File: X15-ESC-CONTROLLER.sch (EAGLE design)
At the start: 27 parts, among them IC1 OP-AMP, J1 3V3 -SWCLK-GND-SWDIO- NRST, Y1 ECS-80-S-4X

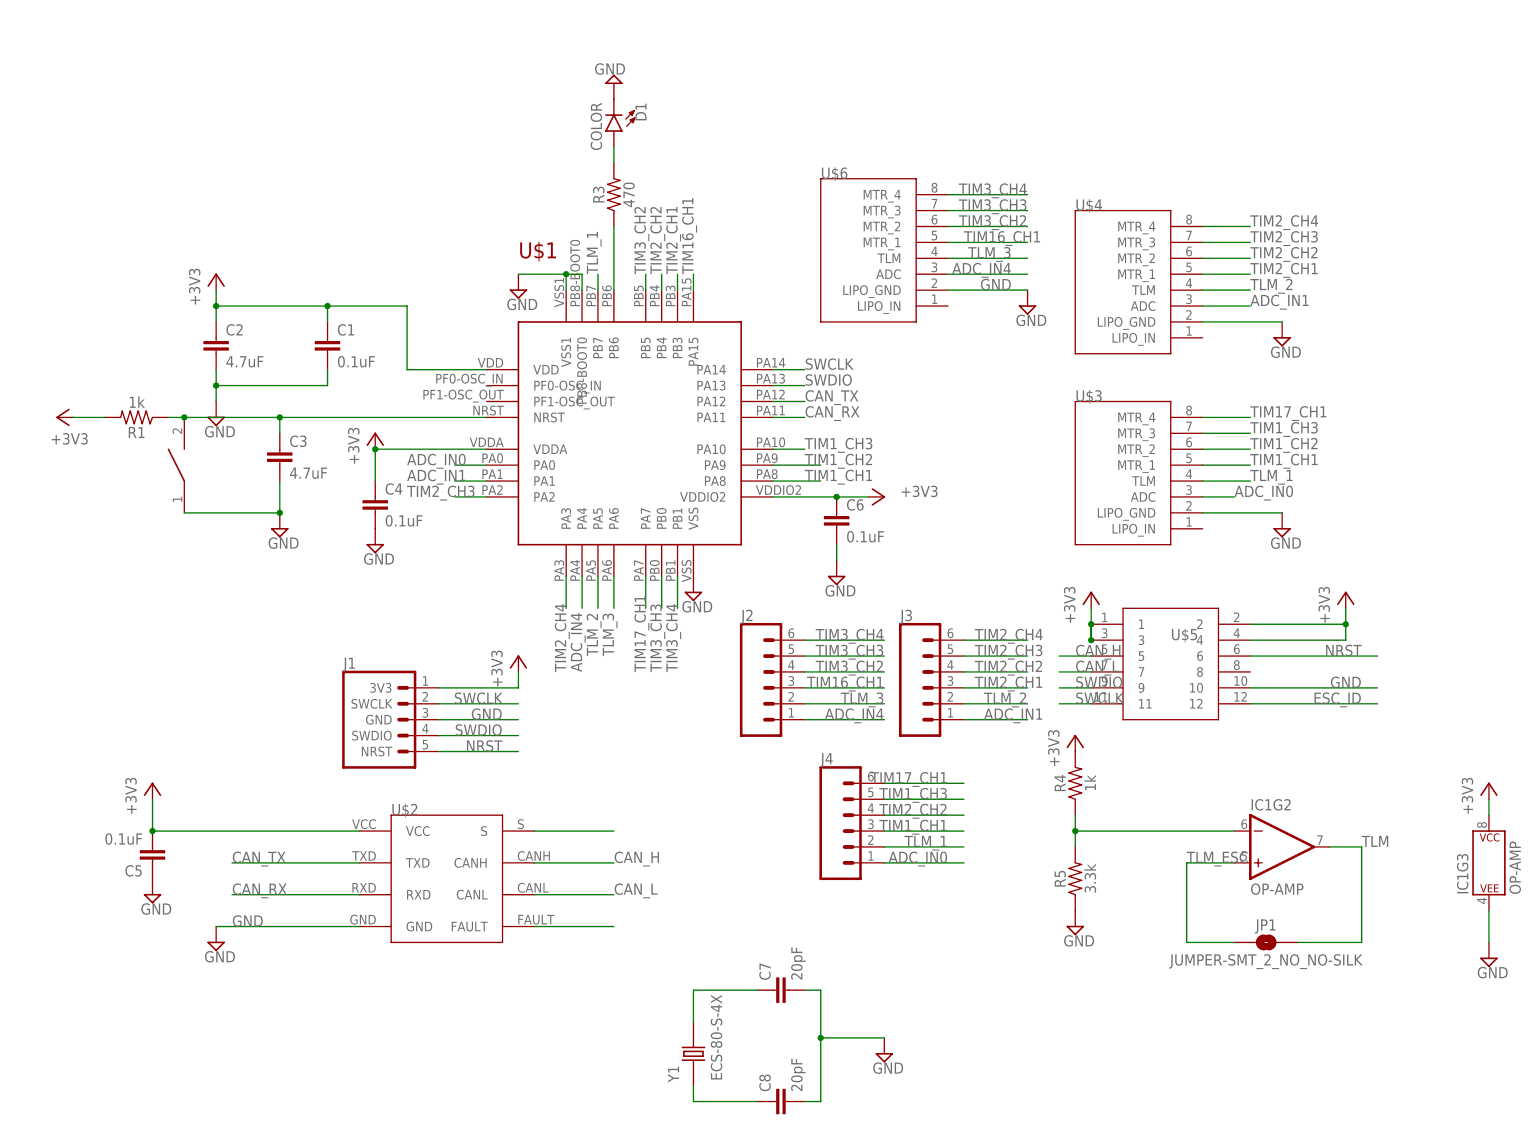
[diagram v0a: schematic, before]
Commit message: Fix some traces with polygons
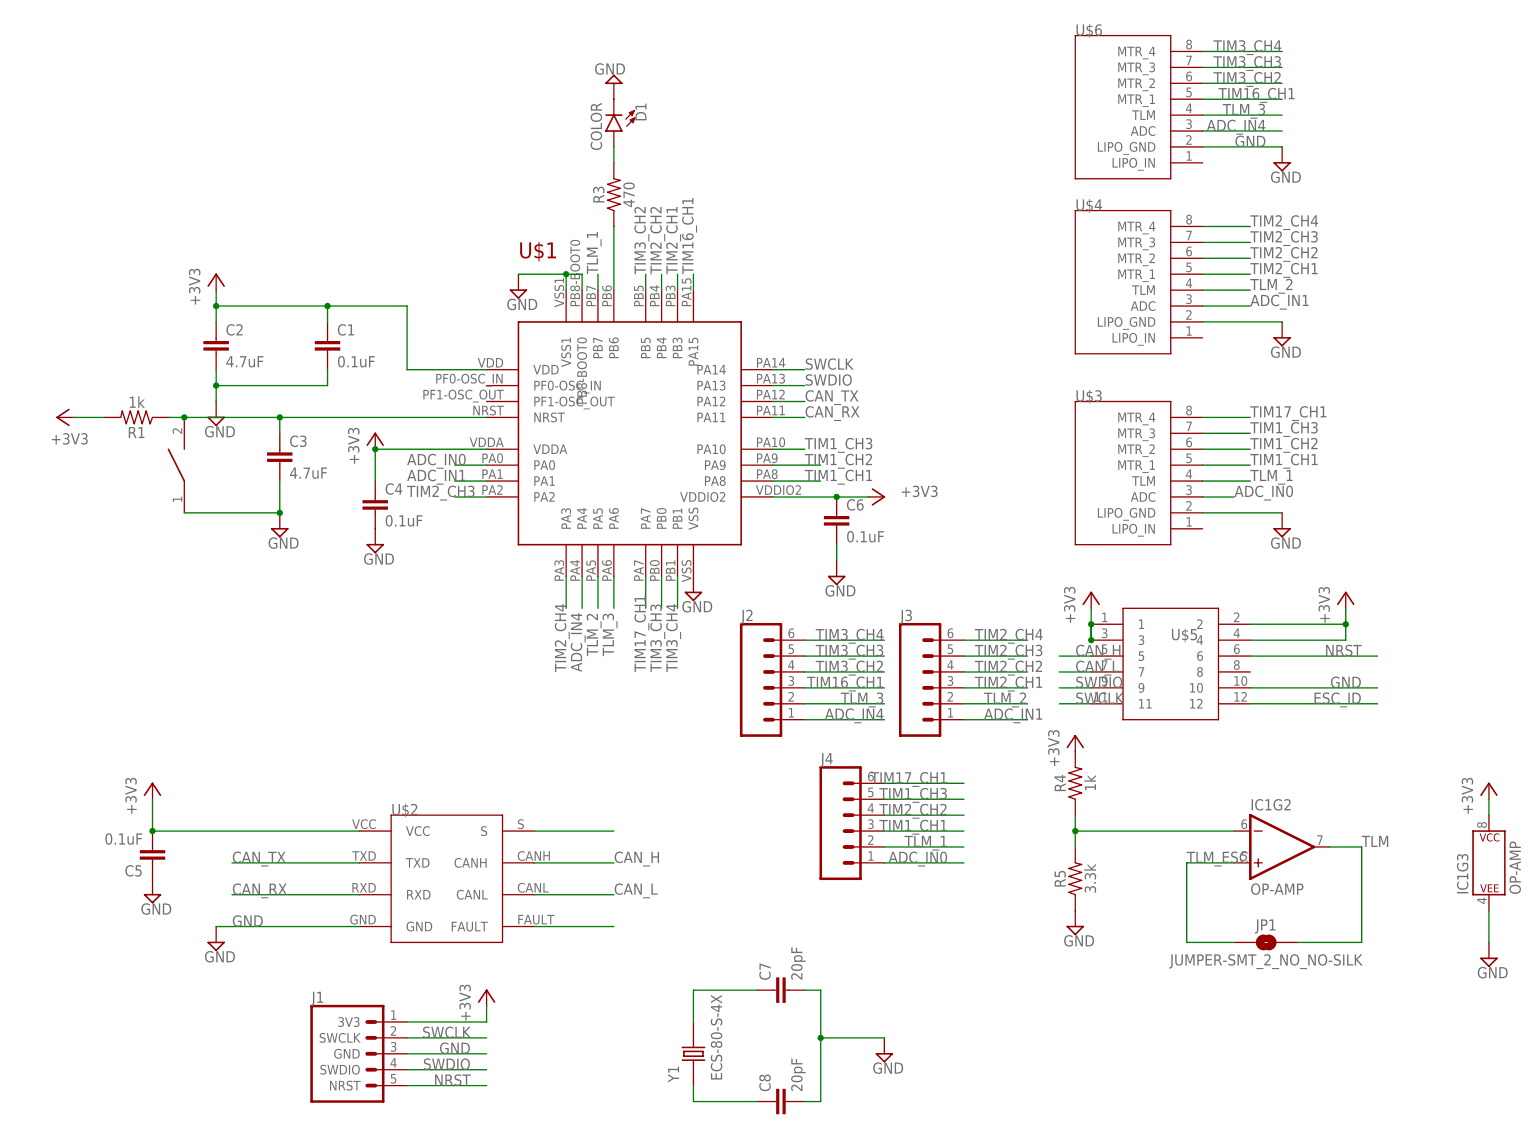
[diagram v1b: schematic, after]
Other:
- moved on the sheet: J1, U$6
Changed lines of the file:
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@@
 <attribute name="VALUE" x="-60.325" y="1.905" size="1.778" layer="96"/>
 </instance>
-<instance part="J1" gate="G$1" x="-20.32" y="33.02" smashed="yes">
-<attribute name="NAME" x="-27.94" y="41.148" size="1.778" layer="95" font="vector"/>
+<instance part="J1" gate="G$1" x="-25.4" y="-20.32" smashed="yes">
+<attribute name="NAME" x="-33.02" y="-12.192" size="1.778" layer="95" font="vector"/>
 </instance>
 <instance part="+3V5" gate="G$1" x="58.42" y="68.58" smashed="yes" rot="R270">
@@
 <attribute name="VALUE" x="153.035" y="-8.255" size="1.778" layer="96"/>
 </instance>
-<instance part="+3V11" gate="G$1" x="0" y="43.18" smashed="yes">
-<attribute name="VALUE" x="-2.54" y="38.1" size="1.778" layer="96" rot="R90"/>
-</instance>
-<instance part="U$6" gate="G$1" x="55.88" y="106.68" smashed="yes">
-<attribute name="NAME" x="48.26" y="119.38" size="1.778" layer="95"/>
-</instance>
-<instance part="SUPPLY15" gate="GND" x="81.28" y="99.06" smashed="yes">
-<attribute name="VALUE" x="79.375" y="95.885" size="1.778" layer="96"/>
+<instance part="+3V11" gate="G$1" x="-5.08" y="-10.16" smashed="yes">
+<attribute name="VALUE" x="-7.62" y="-15.24" size="1.778" layer="96" rot="R90"/>
+</instance>
+<instance part="U$6" gate="G$1" x="96.52" y="129.54" smashed="yes">
+<attribute name="NAME" x="88.9" y="142.24" size="1.778" layer="95"/>
+</instance>
+<instance part="SUPPLY15" gate="GND" x="121.92" y="121.92" smashed="yes">
+<attribute name="VALUE" x="120.015" y="118.745" size="1.778" layer="96"/>
 </instance>
 <instance part="Y1" gate="G$1" x="27.94" y="-20.32" smashed="yes" rot="R90">
@@
 <segment>
 <pinref part="J1" gate="G$1" pin="3V3"/>
-<wire x1="-12.7" y1="38.1" x2="0" y2="38.1" width="0.1524" layer="91"/>
+<wire x1="-17.78" y1="-15.24" x2="-5.08" y2="-15.24" width="0.1524" layer="91"/>
 <pinref part="+3V11" gate="G$1" pin="+3V3"/>
-<wire x1="0" y1="40.64" x2="0" y2="38.1" width="0.1524" layer="91"/>
+<wire x1="-5.08" y1="-12.7" x2="-5.08" y2="-15.24" width="0.1524" layer="91"/>
 </segment>
 <segment>
@@
 <segment>
 <pinref part="J1" gate="G$1" pin="GND"/>
-<wire x1="-12.7" y1="33.02" x2="0" y2="33.02" width="0.1524" layer="91"/>
-<label x="-2.54" y="33.02" size="1.778" layer="95" align="bottom-right"/>
+<wire x1="-17.78" y1="-20.32" x2="-5.08" y2="-20.32" width="0.1524" layer="91"/>
+<label x="-7.62" y="-20.32" size="1.778" layer="95" align="bottom-right"/>
 </segment>
 <segment>
@@
 <segment>
 <pinref part="U$6" gate="G$1" pin="LIPO_GND"/>
-<wire x1="68.58" y1="101.6" x2="81.28" y2="101.6" width="0.1524" layer="91"/>
-<label x="78.74" y="101.6" size="1.778" layer="95" align="bottom-right"/>
+<wire x1="109.22" y1="124.46" x2="121.92" y2="124.46" width="0.1524" layer="91"/>
+<label x="119.38" y="124.46" size="1.778" layer="95" align="bottom-right"/>
 <pinref part="SUPPLY15" gate="GND" pin="GND"/>
 </segment>
@@
 <segment>
 <pinref part="J1" gate="G$1" pin="NRST"/>
-<wire x1="-12.7" y1="27.94" x2="0" y2="27.94" width="0.1524" layer="91"/>
-<label x="-2.54" y="27.94" size="1.778" layer="95" align="bottom-right"/>
+<wire x1="-17.78" y1="-25.4" x2="-5.08" y2="-25.4" width="0.1524" layer="91"/>
+<label x="-7.62" y="-25.4" size="1.778" layer="95" align="bottom-right"/>
 </segment>
 <segment>
@@
 <segment>
 <pinref part="J1" gate="G$1" pin="SWDIO"/>
-<wire x1="-12.7" y1="30.48" x2="0" y2="30.48" width="0.1524" layer="91"/>
-<label x="-2.54" y="30.48" size="1.778" layer="95" align="bottom-right"/>
+<wire x1="-17.78" y1="-22.86" x2="-5.08" y2="-22.86" width="0.1524" layer="91"/>
+<label x="-7.62" y="-22.86" size="1.778" layer="95" align="bottom-right"/>
 </segment>
 <segment>
@@
 <segment>
 <pinref part="J1" gate="G$1" pin="SWCLK"/>
-<wire x1="-12.7" y1="35.56" x2="0" y2="35.56" width="0.1524" layer="91"/>
-<label x="-2.54" y="35.56" size="1.778" layer="95" align="bottom-right"/>
+<wire x1="-17.78" y1="-17.78" x2="-5.08" y2="-17.78" width="0.1524" layer="91"/>
+<label x="-7.62" y="-17.78" size="1.778" layer="95" align="bottom-right"/>
 </segment>
 <segment>
@@
 <segment>
 <pinref part="U$6" gate="G$1" pin="ADC"/>
-<wire x1="68.58" y1="104.14" x2="81.28" y2="104.14" width="0.1524" layer="91"/>
-<label x="78.74" y="104.14" size="1.778" layer="95" align="bottom-right"/>
+<wire x1="109.22" y1="127" x2="121.92" y2="127" width="0.1524" layer="91"/>
+<label x="119.38" y="127" size="1.778" layer="95" align="bottom-right"/>
 </segment>
 <segment>
@@
 <segment>
 <pinref part="U$6" gate="G$1" pin="TLM"/>
-<wire x1="68.58" y1="106.68" x2="81.28" y2="106.68" width="0.1524" layer="91"/>
-<label x="78.74" y="106.68" size="1.778" layer="95" align="bottom-right"/>
+<wire x1="109.22" y1="129.54" x2="121.92" y2="129.54" width="0.1524" layer="91"/>
+<label x="119.38" y="129.54" size="1.778" layer="95" align="bottom-right"/>
 </segment>
 <segment>
@@
 <segment>
 <pinref part="U$6" gate="G$1" pin="MTR_3"/>
-<wire x1="68.58" y1="114.3" x2="81.28" y2="114.3" width="0.1524" layer="91"/>
-<label x="81.28" y="114.3" size="1.778" layer="95" align="bottom-right"/>
+<wire x1="109.22" y1="137.16" x2="121.92" y2="137.16" width="0.1524" layer="91"/>
+<label x="121.92" y="137.16" size="1.778" layer="95" align="bottom-right"/>
 </segment>
 <segment>
@@
 <segment>
 <pinref part="U$6" gate="G$1" pin="MTR_4"/>
-<wire x1="68.58" y1="116.84" x2="81.28" y2="116.84" width="0.1524" layer="91"/>
-<label x="81.28" y="116.84" size="1.778" layer="95" align="bottom-right"/>
+<wire x1="109.22" y1="139.7" x2="121.92" y2="139.7" width="0.1524" layer="91"/>
+<label x="121.92" y="139.7" size="1.778" layer="95" align="bottom-right"/>
 </segment>
 <segment>
@@
 <segment>
 <pinref part="U$6" gate="G$1" pin="MTR_2"/>
-<wire x1="68.58" y1="111.76" x2="81.28" y2="111.76" width="0.1524" layer="91"/>
-<label x="81.28" y="111.76" size="1.778" layer="95" align="bottom-right"/>
+<wire x1="109.22" y1="134.62" x2="121.92" y2="134.62" width="0.1524" layer="91"/>
+<label x="121.92" y="134.62" size="1.778" layer="95" align="bottom-right"/>
 </segment>
 <segment>
@@
 <segment>
 <pinref part="U$6" gate="G$1" pin="MTR_1"/>
-<wire x1="68.58" y1="109.22" x2="81.28" y2="109.22" width="0.1524" layer="91"/>
-<label x="71.12" y="109.22" size="1.778" layer="95"/>
-</segment>
-<segment>
+<wire x1="109.22" y1="132.08" x2="121.92" y2="132.08" width="0.1524" layer="91"/>
+<label x="111.76" y="132.08" size="1.778" layer="95"/>
+</segment>
+<segment>

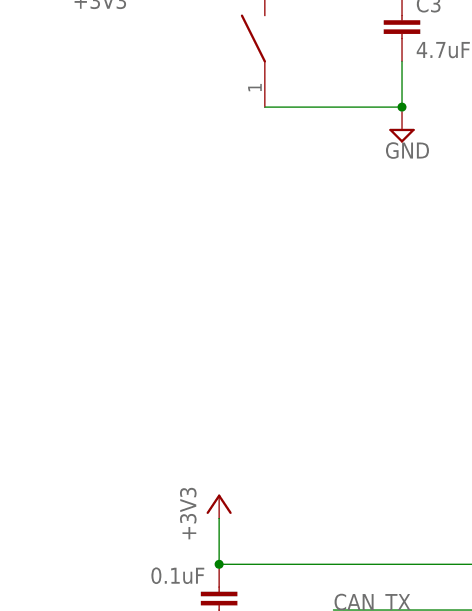
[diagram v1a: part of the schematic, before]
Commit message: Add 3.3V testing LED
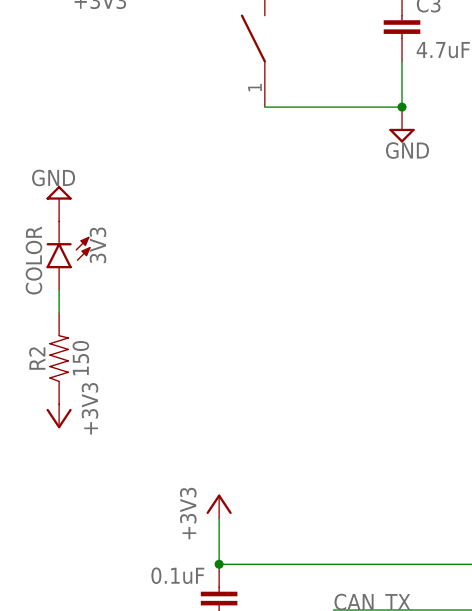
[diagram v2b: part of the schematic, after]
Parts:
- added 3V3: COLOR, X15-ESC-Controller-Parts-Library:LED-0805
- added R2: 150, SparkFun-Resistors:1KOHM-0603-1/10W-1%
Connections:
- new net N$1: 3V3.A, R2.2
- net +3V3: now also R2.1
- net GND: now also 3V3.C
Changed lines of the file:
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@@
 <part name="U$7" library="X15-ESC-Controller-Parts-Library" deviceset="DISCRETECOMPONENTS_SWITCH" device="" package3d_urn="urn:adsk.eagle:package:24384574/2"/>
 <part name="D1" library="X15-ESC-Controller-Parts-Library" deviceset="LED-0805" device="" value="COLOR"/>
+<part name="3V3" library="X15-ESC-Controller-Parts-Library" deviceset="LED-0805" device="" value="COLOR"/>
+<part name="R2" library="SparkFun-Resistors" deviceset="1KOHM" device="-0603-1/10W-1%" value="150"/>
+<part name="+3V3" library="supply1" library_urn="urn:adsk.eagle:library:371" deviceset="+3V3" device=""/>
+<part name="SUPPLY16" library="supply2" library_urn="urn:adsk.eagle:library:372" deviceset="GND" device=""/>
 </parts>
 <sheets>
@@
 <attribute name="NAME" x="18.669" y="131.572" size="1.778" layer="95" font="vector" rot="R270"/>
 <attribute name="VALUE" x="13.335" y="131.572" size="1.778" layer="96" font="vector" rot="R270" align="top-left"/>
+</instance>
+<instance part="3V3" gate="G$1" x="-76.2" y="48.26" smashed="yes" rot="R180">
+<attribute name="NAME" x="-72.771" y="52.832" size="1.778" layer="95" font="vector" rot="R270"/>
+<attribute name="VALUE" x="-78.105" y="52.832" size="1.778" layer="96" font="vector" rot="R270" align="top-left"/>
+</instance>
+<instance part="R2" gate="G$1" x="-76.2" y="38.1" smashed="yes" rot="R90">
+<attribute name="NAME" x="-77.724" y="38.1" size="1.778" layer="95" font="vector" rot="R90" align="bottom-center"/>
+<attribute name="VALUE" x="-74.676" y="38.1" size="1.778" layer="96" font="vector" rot="R90" align="top-center"/>
+</instance>
+<instance part="+3V3" gate="G$1" x="-76.2" y="30.48" smashed="yes" rot="R180">
+<attribute name="VALUE" x="-73.66" y="35.56" size="1.778" layer="96" rot="R270"/>
+</instance>
+<instance part="SUPPLY16" gate="GND" x="-76.2" y="55.88" smashed="yes" rot="R180">
+<attribute name="VALUE" x="-74.295" y="59.055" size="1.778" layer="96" rot="R180"/>
 </instance>
 </instances>
@@
 <junction x="-48.26" y="99.06"/>
 </segment>
+<segment>
+<pinref part="R2" gate="G$1" pin="1"/>
+<pinref part="+3V3" gate="G$1" pin="+3V3"/>
+</segment>
 </net>
 <net name="GND" class="0">
@@
 <pinref part="SUPPLY9" gate="GND" pin="GND"/>
 <pinref part="D1" gate="G$1" pin="C"/>
+</segment>
+<segment>
+<pinref part="3V3" gate="G$1" pin="C"/>
+<pinref part="SUPPLY16" gate="GND" pin="GND"/>
 </segment>
 </net>
@@
 </segment>
 </net>
+<net name="N$1" class="0">
+<segment>
+<pinref part="R2" gate="G$1" pin="2"/>
+<pinref part="3V3" gate="G$1" pin="A"/>
+<wire x1="-76.2" y1="43.18" x2="-76.2" y2="45.72" width="0.1524" layer="91"/>
+</segment>
+</net>

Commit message: Complete Board
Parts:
- JP1: value JUMPER-SMT_2_NO_NO-SILK -> JUMPER-SMT
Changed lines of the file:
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@@
 <part name="+3V8" library="supply1" library_urn="urn:adsk.eagle:library:371" deviceset="+3V3" device=""/>
 <part name="IC1" library="SparkFun-IC-Amplifiers" deviceset="OPAMP-DUAL" device="U" value="OP-AMP"/>
-<part name="JP1" library="SparkFun-Jumpers" deviceset="JUMPER-SMT_2_NO" device="_NO-SILK" package3d_urn="urn:adsk.eagle:package:39277/1"/>
+<part name="JP1" library="SparkFun-Jumpers" deviceset="JUMPER-SMT_2_NO" device="_NO-SILK" package3d_urn="urn:adsk.eagle:package:39277/1" value="JUMPER-SMT"/>
 <part name="R4" library="SparkFun-Resistors" deviceset="1KOHM" device="-0603-1/10W-1%" value="1k"/>
 <part name="R5" library="SparkFun-Resistors" deviceset="1KOHM" device="-0603-1/10W-1%" value="3.3k"/>
@@
 </drawing>
 <compatibility>
-<note version="6.3" minversion="6.2.2" severity="warning">
-Since Version 6.2.2 text objects can contain more than one line,
-which will not be processed correctly with this version.
-</note>
 <note version="8.2" severity="warning">
 Since Version 8.2, EAGLE supports online libraries. The ids

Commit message: Design X15 ESC Controller Again
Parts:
- removed 3V3: COLOR, X15-ESC-Controller-Parts-Library:LED-0805
- removed IC1: OP-AMP, SparkFun-IC-Amplifiers:OPAMP-DUALU
- removed JP1: JUMPER-SMT, SparkFun-Jumpers:JUMPER-SMT_2_NO_NO-SILK
- added D2: FAULT, LED-0805:LED-0805
- added D3: PWR, X15-ESC-Controller-Parts-Library:LED-0805
- added J5: (no value), SparkFun-Connectors:CONN_03
- added J6: (no value), SparkFun-Connectors:CONN_02
- added Q4: 220mA/50V/3.5Ω, SparkFun-DiscreteSemi:MOSFET-NCH-BSS138
- added R6, R7: 0, SparkFun-Resistors:1KOHM-0603-1/10W-1%
- C1, C4, C5, C6: value 0.1uF -> 0.1u
- C2, C3: value 4.7uF -> 4.7u
- C7, C8: value 20pF -> 20p; device SparkFun-Capacitors:20PF-0402T-50V-5% -> SparkFun-Capacitors:22PF-0603-50V-5%
- D1: value COLOR -> PROG
- J1: value 3V3 -SWCLK-GND-SWDIO- NRST -> (none); device X15-ESC-Controller-Parts-Library:SWD_CONN -> SparkFun-Connectors:CONN_05
- J2, J3: device SparkFun-Connectors:CONN_06NO_SILK_NO_POP -> SparkFun-Connectors:CONN_04
- J4: device SparkFun-Connectors:CONN_06NO_SILK_NO_POP -> SparkFun-Connectors:CONN_03
- R3: value 470 -> 150
- R4: device SparkFun-Resistors:1KOHM-0603-1/10W-1% -> SparkFun-Resistors:RESISTOR0603
- R5: value 3.3k -> 100; device SparkFun-Resistors:1KOHM-0603-1/10W-1% -> SparkFun-Resistors:RESISTOR0603
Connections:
- net CAN_H renamed CAN_P
- net CAN_L renamed CAN_N
- net N$4 renamed PROG_LED
- removed net ADC_IN0: J4.1, U$1.PA0, U$3.ADC
- removed net ADC_IN1: J3.1, U$1.PA1, U$4.ADC
- removed net ADC_IN4: J2.1, U$1.PA4, U$6.ADC
- removed net ESC_ID: U$5.12
- removed net N$12: U$2.FAULT
- removed net N$6: C7.1, Y1.2
- removed net N$9: U$2.S
- removed net TIM1_CH1: J4.3, U$1.PA8, U$3.MTR_1
- removed net TIM1_CH2: U$1.PA9, U$3.MTR_2
- removed net TIM1_CH3: J4.5, U$1.PA10, U$3.MTR_3
- removed net TLM: IC1G2.OUT, JP1.2
- removed net TLM_ESC: IC1G2.+IN, JP1.1
- new net FAULT: Q4.G, R4.1, U$2.FAULT
- new net N$4: C7.1, R6.1, Y1.2
- new net OSC_IN: R7.2, U$1.PF0-OSC_IN
- new net OSC_OUT: R6.2, U$1.PF1-OSC_OUT
- new net TIM14_CH1: J4.1, U$1.PA4, U$6.MTR_1
- new net TIM3_CH1: J3.1, U$1.PB4, U$4.MTR_1
- net +3V3: now also J1.5, J6.2, R5.2; no longer IC1G3.P$V+, J1.3V3
- net GND: now also D3.C, J1.3, J6.1, Q4.S; no longer 3V3.C, IC1G3.P$V-, J1.GND, R5.1
- net N$1: now also D3.A; no longer 3V3.A
- net N$2: now also D2.C, Q4.D; no longer C3.1, R1.1, U$1.NRST, U$7.P$2
- net N$3: now also D2.A, R5.1; no longer IC1G2.-IN, R4.1, R5.2
- net N$7: now also R7.1
- net NRST: now also C3.1, J1.1, R1.1, U$1.NRST, U$7.P$2; no longer J1.NRST
- net SWCLK: now also J1.4; no longer J1.SWCLK
- net SWDIO: now also J1.2; no longer J1.SWDIO
- net TIM16_CH1: now also J4.2, U$1.PA6, U$6.MTR_2; no longer J2.3, U$1.PA15, U$6.MTR_1
- net TIM17_CH1: now also J4.3, U$6.MTR_3; no longer J4.6, U$3.MTR_4
- net TIM2_CH1: now also J2.1, U$1.PA0, U$3.MTR_1; no longer J3.3, U$1.PB3, U$4.MTR_1
- net TIM2_CH2: now also J2.2, U$1.PA1, U$3.MTR_2; no longer J3.4, J4.4, U$1.PB4, U$4.MTR_2
- net TIM2_CH3: now also J2.3, U$3.MTR_3; no longer J3.5, U$4.MTR_3
- net TIM2_CH4: now also J2.4, U$3.MTR_4; no longer J3.6, U$4.MTR_4
- net TIM3_CH2: now also J3.2, U$4.MTR_2; no longer J2.4, U$6.MTR_2
- net TIM3_CH3: now also J3.3, U$4.MTR_3; no longer J2.5, U$6.MTR_3
- net TIM3_CH4: now also J3.4, U$4.MTR_4; no longer J2.6, U$6.MTR_4
- net TLM_1: now also J5.1; no longer J4.2, U$1.PB7
- net TLM_2: now also J5.2; no longer J3.2, U$1.PA5
- net TLM_3: now also J5.3; no longer J2.2, U$1.PA6
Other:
- note added: "Backplane Connector"
- note added: "CAN Fault"
- note added: "CAN Transceiver"
- note added: "Connectors + LED"
- note added: "Decoupling Capacitors"
- note added: "Decoupling capacitors for STM32 and CAN Transceiver"
- note added: "ESC JST Connector"
- note added: "External Oscillator"
- note added: "Indicating LED"
- note added: "NRST Button"
- note added: "Program Header Pins"
- note added: "STM32 + CAN"
- note added: "STM32 Nucleo"
- note added: "Telemetry Test Points"
- note added: "Timer Channels Test Points"
